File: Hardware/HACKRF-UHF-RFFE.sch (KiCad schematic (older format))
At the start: 2 parts, among them J1 SMA_Wurth_60312242114510, J2 SMA_Wurth_60312242114510

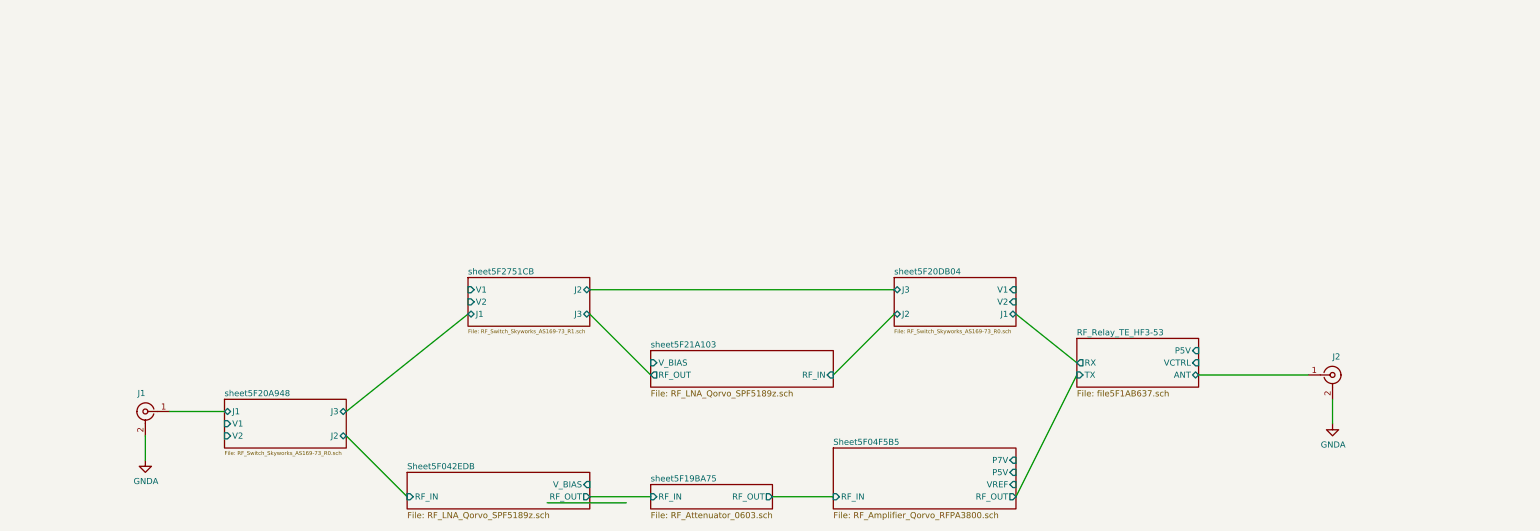
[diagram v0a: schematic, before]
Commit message: Added discrete Chebyshev input filter to schematic based on Qucs simulationd. Artwork not done. It has occurred to me that I need to do some major cleanup of the test points on this PCBA.
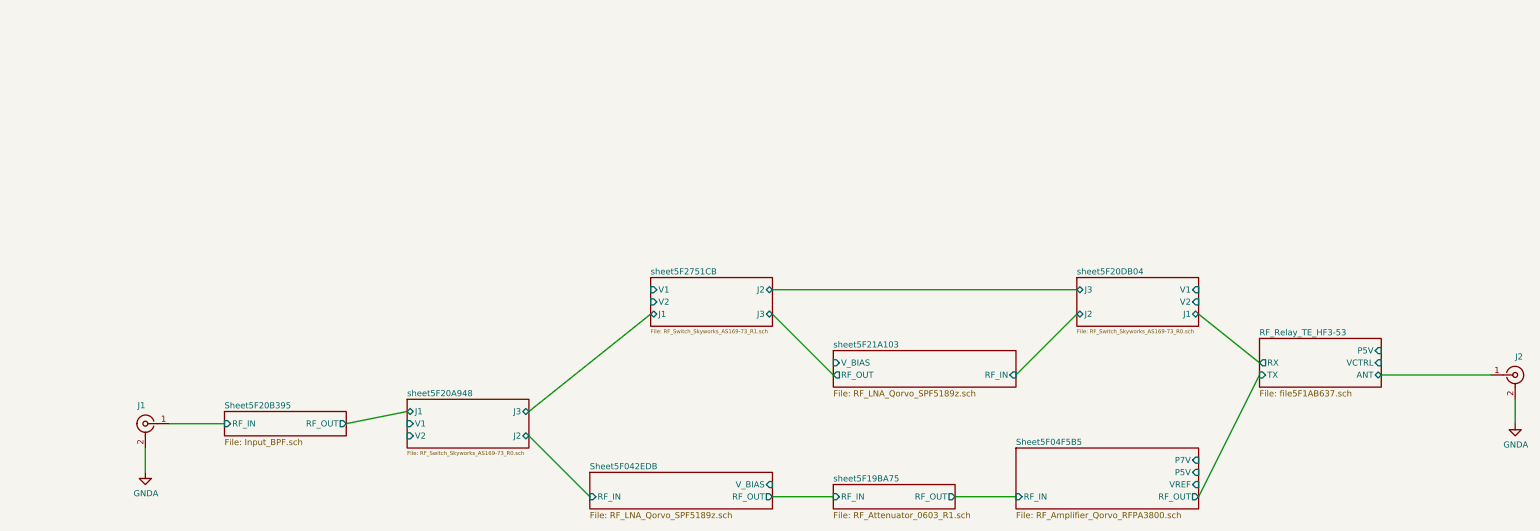
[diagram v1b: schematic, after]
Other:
- moved on the sheet: J1, J2
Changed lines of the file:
@@
 $Descr User 17000 11000
 encoding utf-8
-Sheet 1 12
+Sheet 1 16
 Title "HackRF One Frontend"
 Date "2020-07-04"
@@
 $EndDescr
 Wire Wire Line
-	4050 5200 4500 5200
+	4050 5300 4500 5300
 $Sheet
-S 11500 4600 1000 400
+S 13000 4600 1000 400
 U 5F1AB638
 F0 "RF_Relay_TE_HF3-53" 50
 F1 "file5F1AB637.sch" 50
-F2 "VCTRL" I R 12500 4800 50
-F3 "RX" O L 11500 4800 50
-F4 "TX" I L 11500 4900 50
-F5 "ANT" B R 12500 4900 50
-F6 "P5V" I R 12500 4700 50
+F2 "VCTRL" I R 14000 4800 50
+F3 "RX" O L 13000 4800 50
+F4 "TX" I L 13000 4900 50
+F5 "ANT" B R 14000 4900 50
+F6 "P5V" I R 14000 4700 50
 $EndSheet
 Wire Wire Line
-	13400 4900 12500 4900
+	14900 4900 14000 4900
 $Sheet
-S 8000 5800 1000 200
-U 5F19BA77
-F0 "sheet5F19BA75" 50
-F1 "RF_Attenuator_0603.sch" 50
-F2 "RF_IN" I L 8000 5900 50
-F3 "RF_OUT" O R 9000 5900 50
-$EndSheet
-$Sheet
-S 9500 5500 1500 500
+S 11000 5500 1500 500
 U 5F04F5B6
 F0 "Sheet5F04F5B5" 50
 F1 "RF_Amplifier_Qorvo_RFPA3800.sch" 50
-F2 "RF_IN" I L 9500 5900 50
-F3 "RF_OUT" O R 11000 5900 50
-F4 "VREF" I R 11000 5800 50
-F5 "P7V" I R 11000 5600 50
-F6 "P5V" I R 11000 5700 50
+F2 "RF_IN" I L 11000 5900 50
+F3 "RF_OUT" O R 12500 5900 50
+F4 "VREF" I R 12500 5800 50
+F5 "P7V" I R 12500 5600 50
+F6 "P5V" I R 12500 5700 50
 $EndSheet
 $Sheet
-S 6000 5700 1500 300
+S 7500 5700 1500 300
 U 5F042EDC
 F0 "Sheet5F042EDB" 50
 F1 "RF_LNA_Qorvo_SPF5189z.sch" 50
-F2 "RF_IN" I L 6000 5900 50
-F3 "V_BIAS" I R 7500 5800 50
-F4 "RF_OUT" O R 7500 5900 50
+F2 "RF_IN" I L 7500 5900 50
+F3 "V_BIAS" I R 9000 5800 50
+F4 "RF_OUT" O R 9000 5900 50
 $EndSheet
 $Sheet
-S 4500 5100 1000 400
+S 6000 5100 1000 400
 U 5F20A94F
 F0 "sheet5F20A948" 50
 F1 "RF_Switch_Skyworks_AS169-73_R0.sch" 32
-F2 "J1" B L 4500 5200 50
-F3 "J3" B R 5500 5200 50
-F4 "J2" B R 5500 5400 50
-F5 "V1" I L 4500 5300 50
-F6 "V2" I L 4500 5400 50
+F2 "J1" B L 6000 5200 50
+F3 "J3" B R 7000 5200 50
+F4 "J2" B R 7000 5400 50
+F5 "V1" I L 6000 5300 50
+F6 "V2" I L 6000 5400 50
 $EndSheet
 Wire Wire Line
-	3850 5400 3850 5600
+	3850 5500 3850 5700
 $Sheet
-S 8000 4700 1500 300
+S 9500 4700 1500 300
 U 5F21A108
 F0 "sheet5F21A103" 50
 F1 "RF_LNA_Qorvo_SPF5189z.sch" 50
-F2 "RF_IN" I R 9500 4900 50
-F3 "V_BIAS" I L 8000 4800 50
-F4 "RF_OUT" O L 8000 4900 50
+F2 "RF_IN" I R 11000 4900 50
+F3 "V_BIAS" I L 9500 4800 50
+F4 "RF_OUT" O L 9500 4900 50
 $EndSheet
 Wire Wire Line
-	7500 4400 8000 4900
+	9000 4400 9500 4900
 Wire Wire Line
-	9500 4900 10000 4400
+	11000 4900 11500 4400
 Wire Wire Line
-	10000 4200 7500 4200
+	11500 4200 9000 4200
 Wire Wire Line
-	5500 5200 6500 4400
+	7000 5200 8000 4400
 Wire Wire Line
-	5500 5400 6000 5900
-Wire Wire Line
-	7500 5900 8000 5900
+	7000 5400 7500 5900
 Wire Wire Line
 	9000 5900 9500 5900
 Wire Wire Line
-	11000 5900 11500 4900
+	10500 5900 11000 5900
 Wire Wire Line
-	11000 4400 11500 4800
+	12500 5900 13000 4900
 Wire Wire Line
-	13600 5100 13600 5300
+	12500 4400 13000 4800
+Wire Wire Line
+	15100 5100 15100 5300
 $Sheet
-S 10000 4100 1000 400
+S 11500 4100 1000 400
 U 5F20DB0B
 F0 "sheet5F20DB04" 50
 F1 "RF_Switch_Skyworks_AS169-73_R0.sch" 32
-F2 "J1" B R 11000 4400 50
-F3 "J3" B L 10000 4200 50
-F4 "J2" B L 10000 4400 50
-F5 "V1" I R 11000 4200 50
-F6 "V2" I R 11000 4300 50
+F2 "J1" B R 12500 4400 50
+F3 "J3" B L 11500 4200 50
+F4 "J2" B L 11500 4400 50
+F5 "V1" I R 12500 4200 50
+F6 "V2" I R 12500 4300 50
 $EndSheet
 $Comp
 L power:GNDA #PWR02
 U 1 1 5F25C5EB
-P 13600 5300
-F 0 "#PWR02" H 13600 5050 50  0001 C CNN
-F 1 "GNDA" H 13605 5127 50  0000 C CNN
-F 2 "" H 13600 5300 50  0001 C CNN
-F 3 "" H 13600 5300 50  0001 C CNN
-	1    13600 5300
+P 15100 5300
+F 0 "#PWR02" H 15100 5050 50  0001 C CNN
+F 1 "GNDA" H 15105 5127 50  0000 C CNN
+F 2 "" H 15100 5300 50  0001 C CNN
+F 3 "" H 15100 5300 50  0001 C CNN
+	1    15100 5300
 	1    0    0    -1
 $EndComp
@@
 L power:GNDA #PWR01
 U 1 1 5F2113AB
-P 3850 5600
-F 0 "#PWR01" H 3850 5350 50  0001 C CNN
-F 1 "GNDA" H 3855 5427 50  0000 C CNN
-F 2 "" H 3850 5600 50  0001 C CNN
-F 3 "" H 3850 5600 50  0001 C CNN
-	1    3850 5600
+P 3850 5700
+F 0 "#PWR01" H 3850 5450 50  0001 C CNN
+F 1 "GNDA" H 3855 5527 50  0000 C CNN
+F 2 "" H 3850 5700 50  0001 C CNN
+F 3 "" H 3850 5700 50  0001 C CNN
+	1    3850 5700
 	1    0    0    -1
 $EndComp
@@
 L RF:SMA_Wurth_60312242114510 J2
 U 1 1 5F1A3F2A
-P 13600 4900
-F 0 "J2" H 13600 5050 50  0000 L CNN
-F 1 "SMA_Wurth_60312242114510" H 13528 5047 50  0001 C CNN
-F 2 "RF:SMA_Wurth_60312242114510" H 13600 4900 50  0001 C CNN
-F 3 "https://www.we-online.de/katalog/datasheet/60312242114510.pdf" H 13600 4900 50  0001 C CNN
-	1    13600 4900
+P 15100 4900
+F 0 "J2" H 15100 5050 50  0000 L CNN
+F 1 "SMA_Wurth_60312242114510" H 15028 5047 50  0001 C CNN
+F 2 "RF:SMA_Wurth_60312242114510" H 15100 4900 50  0001 C CNN
+F 3 "https://www.we-online.de/katalog/datasheet/60312242114510.pdf" H 15100 4900 50  0001 C CNN
+	1    15100 4900
 	1    0    0    -1
 $EndComp
@@
 L RF:SMA_Wurth_60312242114510 J1
 U 1 1 5F199969
-P 3850 5200
-F 0 "J1" H 3850 5350 50  0000 L CNN
-F 1 "SMA_Wurth_60312242114510" H 3778 5347 50  0001 C CNN
-F 2 "RF:SMA_Wurth_60312242114510" H 3850 5200 50  0001 C CNN
-F 3 "https://www.we-online.de/katalog/datasheet/60312242114510.pdf" H 3850 5200 50  0001 C CNN
-	1    3850 5200
+P 3850 5300
+F 0 "J1" H 3850 5450 50  0000 L CNN
+F 1 "SMA_Wurth_60312242114510" H 3778 5447 50  0001 C CNN
+F 2 "RF:SMA_Wurth_60312242114510" H 3850 5300 50  0001 C CNN
+F 3 "https://www.we-online.de/katalog/datasheet/60312242114510.pdf" H 3850 5300 50  0001 C CNN
+	1    3850 5300
 	-1   0    0    -1
 $EndComp
 $Sheet
-S 6500 4100 1000 400
+S 8000 4100 1000 400
 U 5F2751D2
 F0 "sheet5F2751CB" 50
 F1 "RF_Switch_Skyworks_AS169-73_R1.sch" 32
-F2 "J1" B L 6500 4400 50
-F3 "J3" B R 7500 4400 50
-F4 "J2" B R 7500 4200 50
-F5 "V1" I L 6500 4200 50
-F6 "V2" I L 6500 4300 50
+F2 "J1" B L 8000 4400 50
+F3 "J3" B R 9000 4400 50
+F4 "J2" B R 9000 4200 50
+F5 "V1" I L 8000 4200 50
+F6 "V2" I L 8000 4300 50
+$EndSheet
+$Sheet
+S 9500 5800 1000 200
+U 5F19BA77
+F0 "sheet5F19BA75" 50
+F1 "RF_Attenuator_0603_R1.sch" 50
+F2 "RF_IN" I L 9500 5900 50
+F3 "RF_OUT" O R 10500 5900 50
+$EndSheet
+$Sheet
+S 4500 5200 1000 200
+U 5F20B396
+F0 "Sheet5F20B395" 50
+F1 "Input_BPF.sch" 50
+F2 "RF_IN" I L 4500 5300 50
+F3 "RF_OUT" O R 5500 5300 50
 $EndSheet
 Wire Wire Line
-	7150 5950 7800 5950
+	5500 5300 6000 5200
 $EndSCHEMATC

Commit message: Major cleanup to both the schematic and directory structure. Stackup has changed accomodate to 0.65mm trace width. Chebyshev filter lived through the experience in the Qucs simulation; others not checked yet. I do want to re-visit the matching networks of all of the amplifiers as I have developed some good strategies to implement them.
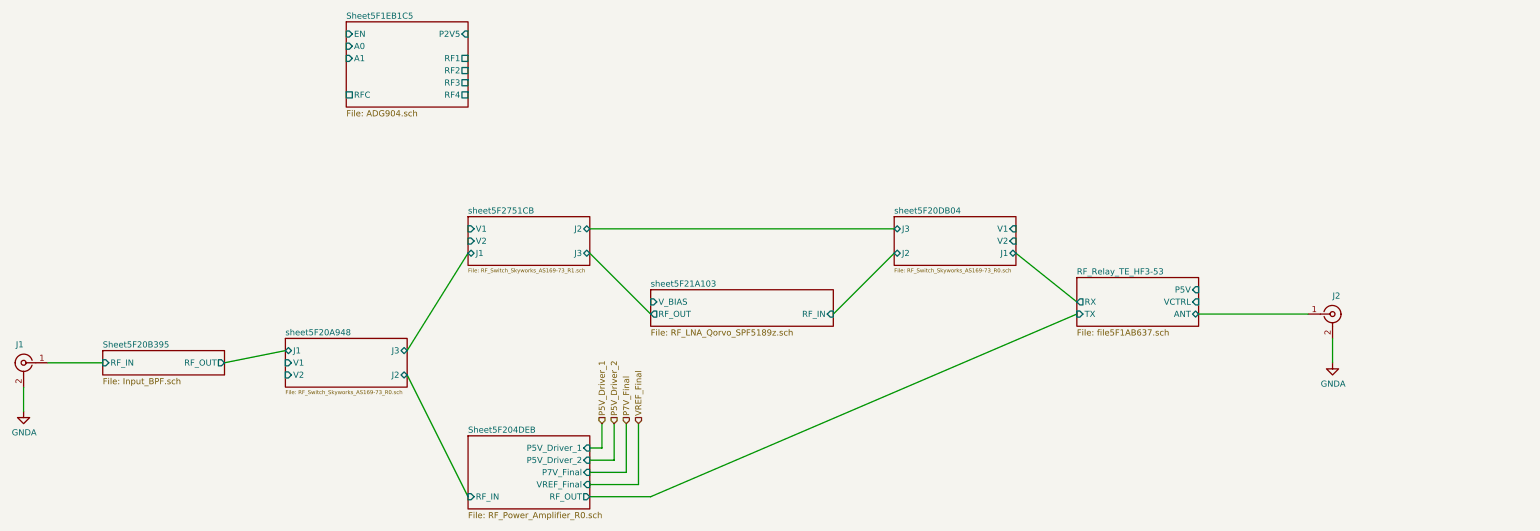
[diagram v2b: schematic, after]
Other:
- moved on the sheet: J1, J2
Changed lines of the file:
@@
 $Descr User 17000 11000
 encoding utf-8
-Sheet 1 16
+Sheet 1 24
 Title "HackRF One Frontend"
 Date "2020-07-04"
@@
 $EndDescr
 Wire Wire Line
-	4050 5300 4500 5300
+	3050 4800 3500 4800
 $Sheet
-S 13000 4600 1000 400
+S 11500 4100 1000 400
 U 5F1AB638
 F0 "RF_Relay_TE_HF3-53" 50
 F1 "file5F1AB637.sch" 50
-F2 "VCTRL" I R 14000 4800 50
-F3 "RX" O L 13000 4800 50
-F4 "TX" I L 13000 4900 50
-F5 "ANT" B R 14000 4900 50
-F6 "P5V" I R 14000 4700 50
+F2 "VCTRL" I R 12500 4300 50
+F3 "RX" O L 11500 4300 50
+F4 "TX" I L 11500 4400 50
+F5 "ANT" B R 12500 4400 50
+F6 "P5V" I R 12500 4200 50
 $EndSheet
 Wire Wire Line
-	14900 4900 14000 4900
+	13400 4400 12500 4400
 $Sheet
-S 11000 5500 1500 500
-U 5F04F5B6
-F0 "Sheet5F04F5B5" 50
-F1 "RF_Amplifier_Qorvo_RFPA3800.sch" 50
-F2 "RF_IN" I L 11000 5900 50
-F3 "RF_OUT" O R 12500 5900 50
-F4 "VREF" I R 12500 5800 50
-F5 "P7V" I R 12500 5600 50
-F6 "P5V" I R 12500 5700 50
-$EndSheet
-$Sheet
-S 7500 5700 1500 300
-U 5F042EDC
-F0 "Sheet5F042EDB" 50
-F1 "RF_LNA_Qorvo_SPF5189z.sch" 50
-F2 "RF_IN" I L 7500 5900 50
-F3 "V_BIAS" I R 9000 5800 50
-F4 "RF_OUT" O R 9000 5900 50
-$EndSheet
-$Sheet
-S 6000 5100 1000 400
+S 5000 4600 1000 400
 U 5F20A94F
 F0 "sheet5F20A948" 50
 F1 "RF_Switch_Skyworks_AS169-73_R0.sch" 32
-F2 "J1" B L 6000 5200 50
-F3 "J3" B R 7000 5200 50
-F4 "J2" B R 7000 5400 50
-F5 "V1" I L 6000 5300 50
-F6 "V2" I L 6000 5400 50
+F2 "J1" B L 5000 4700 50
+F3 "J3" B R 6000 4700 50
+F4 "J2" B R 6000 4900 50
+F5 "V1" I L 5000 4800 50
+F6 "V2" I L 5000 4900 50
 $EndSheet
 Wire Wire Line
-	3850 5500 3850 5700
+	2850 5000 2850 5200
 $Sheet
-S 9500 4700 1500 300
+S 8000 4200 1500 300
 U 5F21A108
 F0 "sheet5F21A103" 50
 F1 "RF_LNA_Qorvo_SPF5189z.sch" 50
-F2 "RF_IN" I R 11000 4900 50
-F3 "V_BIAS" I L 9500 4800 50
-F4 "RF_OUT" O L 9500 4900 50
+F2 "RF_IN" I R 9500 4400 50
+F3 "V_BIAS" I L 8000 4300 50
+F4 "RF_OUT" O L 8000 4400 50
 $EndSheet
 Wire Wire Line
-	9000 4400 9500 4900
+	9500 4400 10000 3900
 Wire Wire Line
-	11000 4900 11500 4400
+	11000 3900 11500 4300
 Wire Wire Line
-	11500 4200 9000 4200
-Wire Wire Line
-	7000 5200 8000 4400
-Wire Wire Line
-	7000 5400 7500 5900
-Wire Wire Line
-	9000 5900 9500 5900
-Wire Wire Line
-	10500 5900 11000 5900
-Wire Wire Line
-	12500 5900 13000 4900
-Wire Wire Line
-	12500 4400 13000 4800
-Wire Wire Line
-	15100 5100 15100 5300
+	13600 4600 13600 4800
 $Sheet
-S 11500 4100 1000 400
+S 10000 3600 1000 400
 U 5F20DB0B
 F0 "sheet5F20DB04" 50
 F1 "RF_Switch_Skyworks_AS169-73_R0.sch" 32
-F2 "J1" B R 12500 4400 50
-F3 "J3" B L 11500 4200 50
-F4 "J2" B L 11500 4400 50
-F5 "V1" I R 12500 4200 50
-F6 "V2" I R 12500 4300 50
+F2 "J1" B R 11000 3900 50
+F3 "J3" B L 10000 3700 50
+F4 "J2" B L 10000 3900 50
+F5 "V1" I R 11000 3700 50
+F6 "V2" I R 11000 3800 50
 $EndSheet
 $Comp
 L power:GNDA #PWR02
 U 1 1 5F25C5EB
-P 15100 5300
-F 0 "#PWR02" H 15100 5050 50  0001 C CNN
-F 1 "GNDA" H 15105 5127 50  0000 C CNN
-F 2 "" H 15100 5300 50  0001 C CNN
-F 3 "" H 15100 5300 50  0001 C CNN
-	1    15100 5300
+P 13600 4800
+F 0 "#PWR02" H 13600 4550 50  0001 C CNN
+F 1 "GNDA" H 13605 4627 50  0000 C CNN
+F 2 "" H 13600 4800 50  0001 C CNN
+F 3 "" H 13600 4800 50  0001 C CNN
+	1    13600 4800
 	1    0    0    -1
 $EndComp
@@
 L power:GNDA #PWR01
 U 1 1 5F2113AB
-P 3850 5700
-F 0 "#PWR01" H 3850 5450 50  0001 C CNN
-F 1 "GNDA" H 3855 5527 50  0000 C CNN
-F 2 "" H 3850 5700 50  0001 C CNN
-F 3 "" H 3850 5700 50  0001 C CNN
-	1    3850 5700
+P 2850 5200
+F 0 "#PWR01" H 2850 4950 50  0001 C CNN
+F 1 "GNDA" H 2855 5027 50  0000 C CNN
+F 2 "" H 2850 5200 50  0001 C CNN
+F 3 "" H 2850 5200 50  0001 C CNN
+	1    2850 5200
 	1    0    0    -1
 $EndComp
@@
 L RF:SMA_Wurth_60312242114510 J2
 U 1 1 5F1A3F2A
-P 15100 4900
-F 0 "J2" H 15100 5050 50  0000 L CNN
-F 1 "SMA_Wurth_60312242114510" H 15028 5047 50  0001 C CNN
-F 2 "RF:SMA_Wurth_60312242114510" H 15100 4900 50  0001 C CNN
-F 3 "https://www.we-online.de/katalog/datasheet/60312242114510.pdf" H 15100 4900 50  0001 C CNN
-	1    15100 4900
+P 13600 4400
+F 0 "J2" H 13600 4550 50  0000 L CNN
+F 1 "SMA_Wurth_60312242114510" H 13528 4547 50  0001 C CNN
+F 2 "RF:SMA_Wurth_60312242114510" H 13600 4400 50  0001 C CNN
+F 3 "https://www.we-online.de/katalog/datasheet/60312242114510.pdf" H 13600 4400 50  0001 C CNN
+	1    13600 4400
 	1    0    0    -1
 $EndComp
@@
 L RF:SMA_Wurth_60312242114510 J1
 U 1 1 5F199969
-P 3850 5300
-F 0 "J1" H 3850 5450 50  0000 L CNN
-F 1 "SMA_Wurth_60312242114510" H 3778 5447 50  0001 C CNN
-F 2 "RF:SMA_Wurth_60312242114510" H 3850 5300 50  0001 C CNN
-F 3 "https://www.we-online.de/katalog/datasheet/60312242114510.pdf" H 3850 5300 50  0001 C CNN
-	1    3850 5300
+P 2850 4800
+F 0 "J1" H 2850 4950 50  0000 L CNN
+F 1 "SMA_Wurth_60312242114510" H 2778 4947 50  0001 C CNN
+F 2 "RF:SMA_Wurth_60312242114510" H 2850 4800 50  0001 C CNN
+F 3 "https://www.we-online.de/katalog/datasheet/60312242114510.pdf" H 2850 4800 50  0001 C CNN
+	1    2850 4800
 	-1   0    0    -1
 $EndComp
 $Sheet
-S 8000 4100 1000 400
+S 6500 3600 1000 400
 U 5F2751D2
 F0 "sheet5F2751CB" 50
 F1 "RF_Switch_Skyworks_AS169-73_R1.sch" 32
-F2 "J1" B L 8000 4400 50
-F3 "J3" B R 9000 4400 50
-F4 "J2" B R 9000 4200 50
-F5 "V1" I L 8000 4200 50
-F6 "V2" I L 8000 4300 50
+F2 "J1" B L 6500 3900 50
+F3 "J3" B R 7500 3900 50
+F4 "J2" B R 7500 3700 50
+F5 "V1" I L 6500 3700 50
+F6 "V2" I L 6500 3800 50
 $EndSheet
 $Sheet
-S 9500 5800 1000 200
-U 5F19BA77
-F0 "sheet5F19BA75" 50
-F1 "RF_Attenuator_0603_R1.sch" 50
-F2 "RF_IN" I L 9500 5900 50
-F3 "RF_OUT" O R 10500 5900 50
-$EndSheet
-$Sheet
-S 4500 5200 1000 200
+S 3500 4700 1000 200
 U 5F20B396
 F0 "Sheet5F20B395" 50
 F1 "Input_BPF.sch" 50
-F2 "RF_IN" I L 4500 5300 50
-F3 "RF_OUT" O R 5500 5300 50
+F2 "RF_IN" I L 3500 4800 50
+F3 "RF_OUT" O R 4500 4800 50
 $EndSheet
 Wire Wire Line
-	5500 5300 6000 5200
+	4500 4800 5000 4700
+$Sheet
+S 6500 5400 1000 600
+U 5F204DEC
+F0 "Sheet5F204DEB" 50
+F1 "RF_Power_Amplifier_R0.sch" 50
+F2 "RF_IN" I L 6500 5900 50
+F3 "RF_OUT" O R 7500 5900 50
+F4 "P5V_Driver_1" I R 7500 5500 50
+F5 "P7V_Final" I R 7500 5700 50
+F6 "P5V_Driver_2" I R 7500 5600 50
+F7 "VREF_Final" I R 7500 5800 50
+$EndSheet
+Wire Wire Line
+	6000 4900 6500 5900
+Wire Wire Line
+	6000 4700 6500 3900
+Wire Wire Line
+	7500 3900 8000 4400
+Wire Wire Line
+	7500 3700 10000 3700
+Wire Wire Line
+	7600 5500 7600 5300
+Wire Wire Line
+	7700 5600 7700 5300
+Wire Wire Line
+	7800 5700 7800 5300
+Wire Wire Line
+	7900 5800 7900 5300
+Text HLabel 7800 5300 1    50   Input ~ 0
+P7V_Final
+Text HLabel 7700 5300 1    50   Input ~ 0
+P5V_Driver_2
+Text HLabel 7900 5300 1    50   Input ~ 0
+VREF_Final
+Text HLabel 7600 5300 1    50   Input ~ 0
+P5V_Driver_1
+Wire Wire Line
+	7500 5500 7600 5500
+Wire Wire Line
+	7500 5600 7700 5600
+Wire Wire Line
+	7500 5700 7800 5700
+Wire Wire Line
+	7500 5800 7900 5800
+Wire Wire Line
+	7500 5900 8000 5900
+Wire Wire Line
+	11500 4400 8000 5900
+$Sheet
+S 5500 2000 1000 700
+U 5F1EB1C6
+F0 "Sheet5F1EB1C5" 50
+F1 "ADG904.sch" 50
+F2 "P2V5" I R 6500 2100 50
+F3 "RF1" U R 6500 2300 50
+F4 "RF2" U R 6500 2400 50
+F5 "RF3" U R 6500 2500 50
+F6 "RF4" U R 6500 2600 50
+F7 "RFC" U L 5500 2600 50
+F8 "EN" I L 5500 2100 50
+F9 "A0" I L 5500 2200 50
+F10 "A1" I L 5500 2300 50
+$EndSheet
 $EndSCHEMATC
